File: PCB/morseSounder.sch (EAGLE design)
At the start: 77 parts, among them IC1 LM386M-1, IC5 LM321MF, J1 AVR_SPI_PRG_6PTH, J2 POWERPOLE_POWER25A_HORIZONTAL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, J3 POWER_JACKPTH, Q1 MMBT3904, Q2 MMBT3904, Q3 MMBT3904, Q4 2.5A/30V/105mΩ, Q5 MMBT3904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

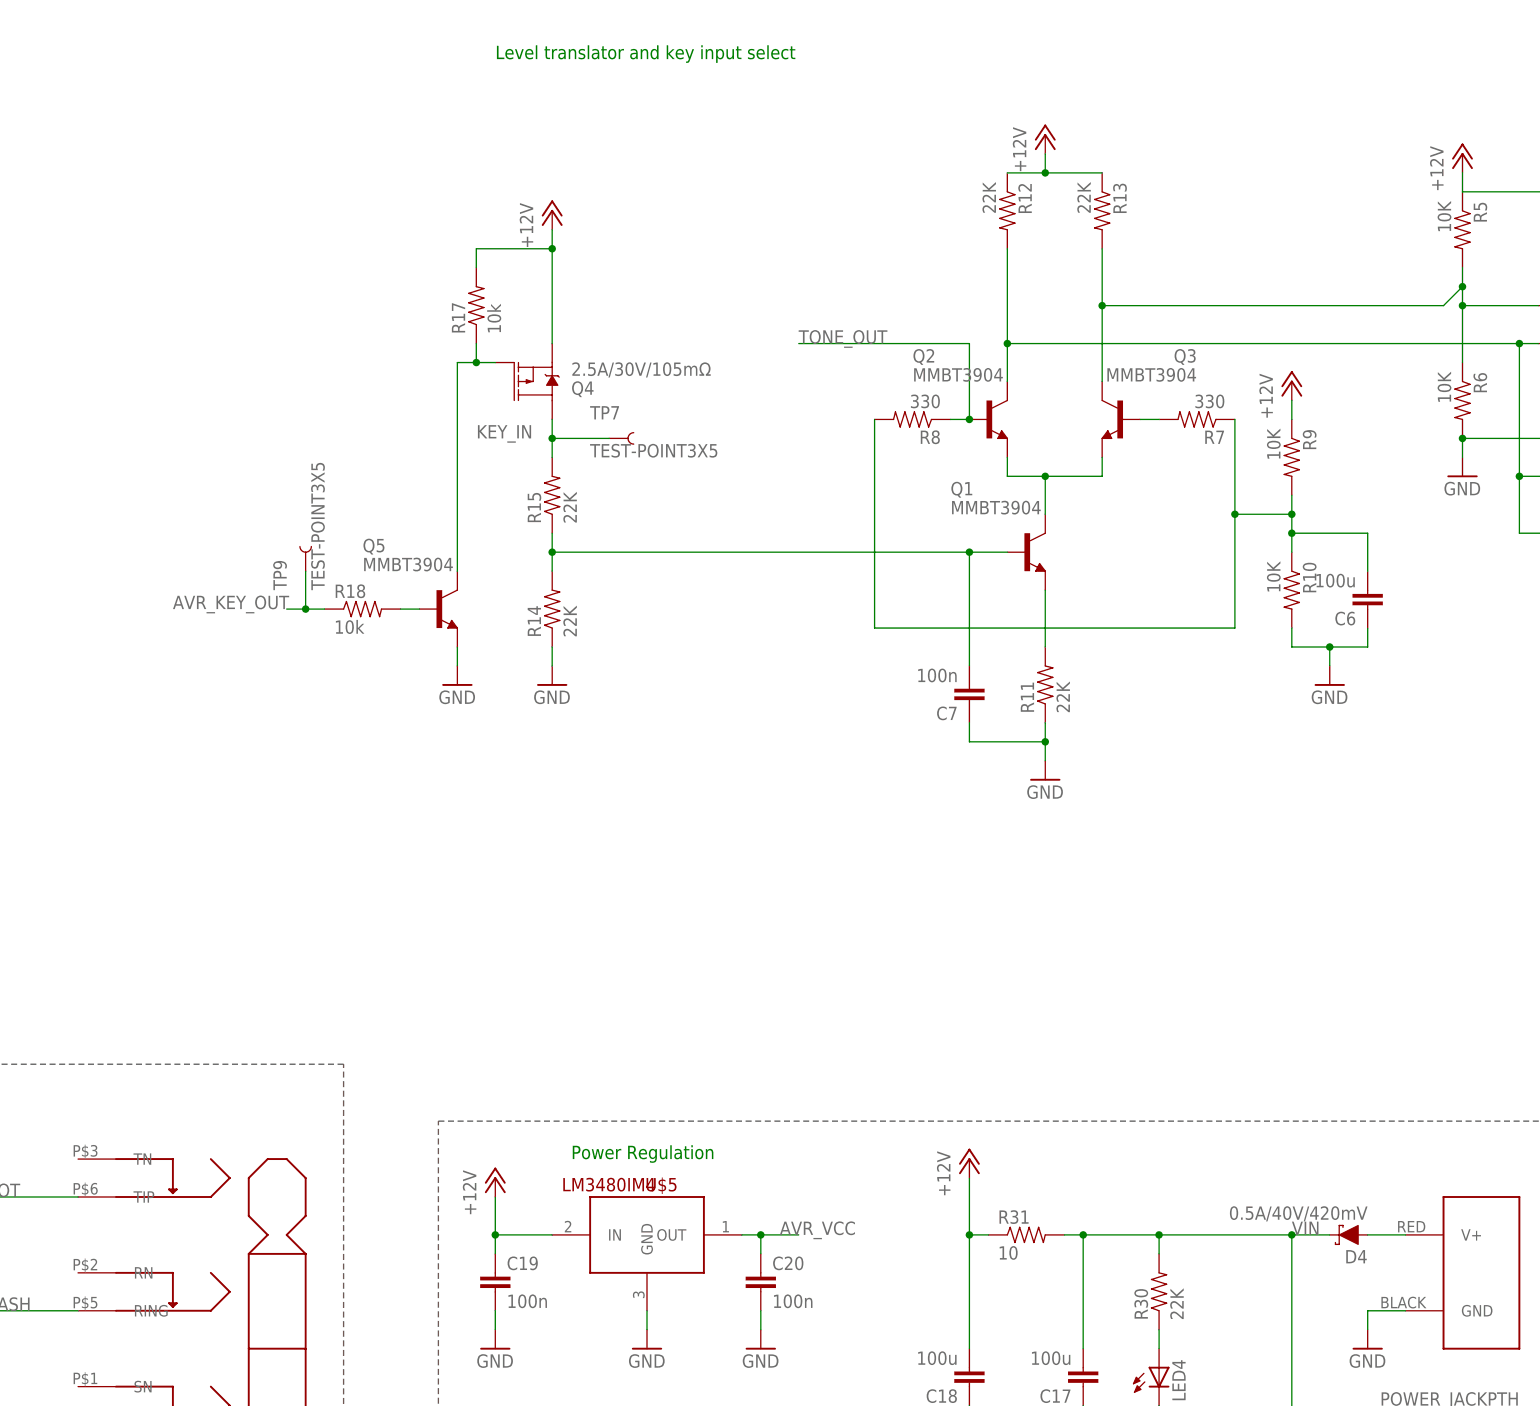
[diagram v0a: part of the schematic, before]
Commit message: * Oops! Power reverse protection diode should protect both power inputs!
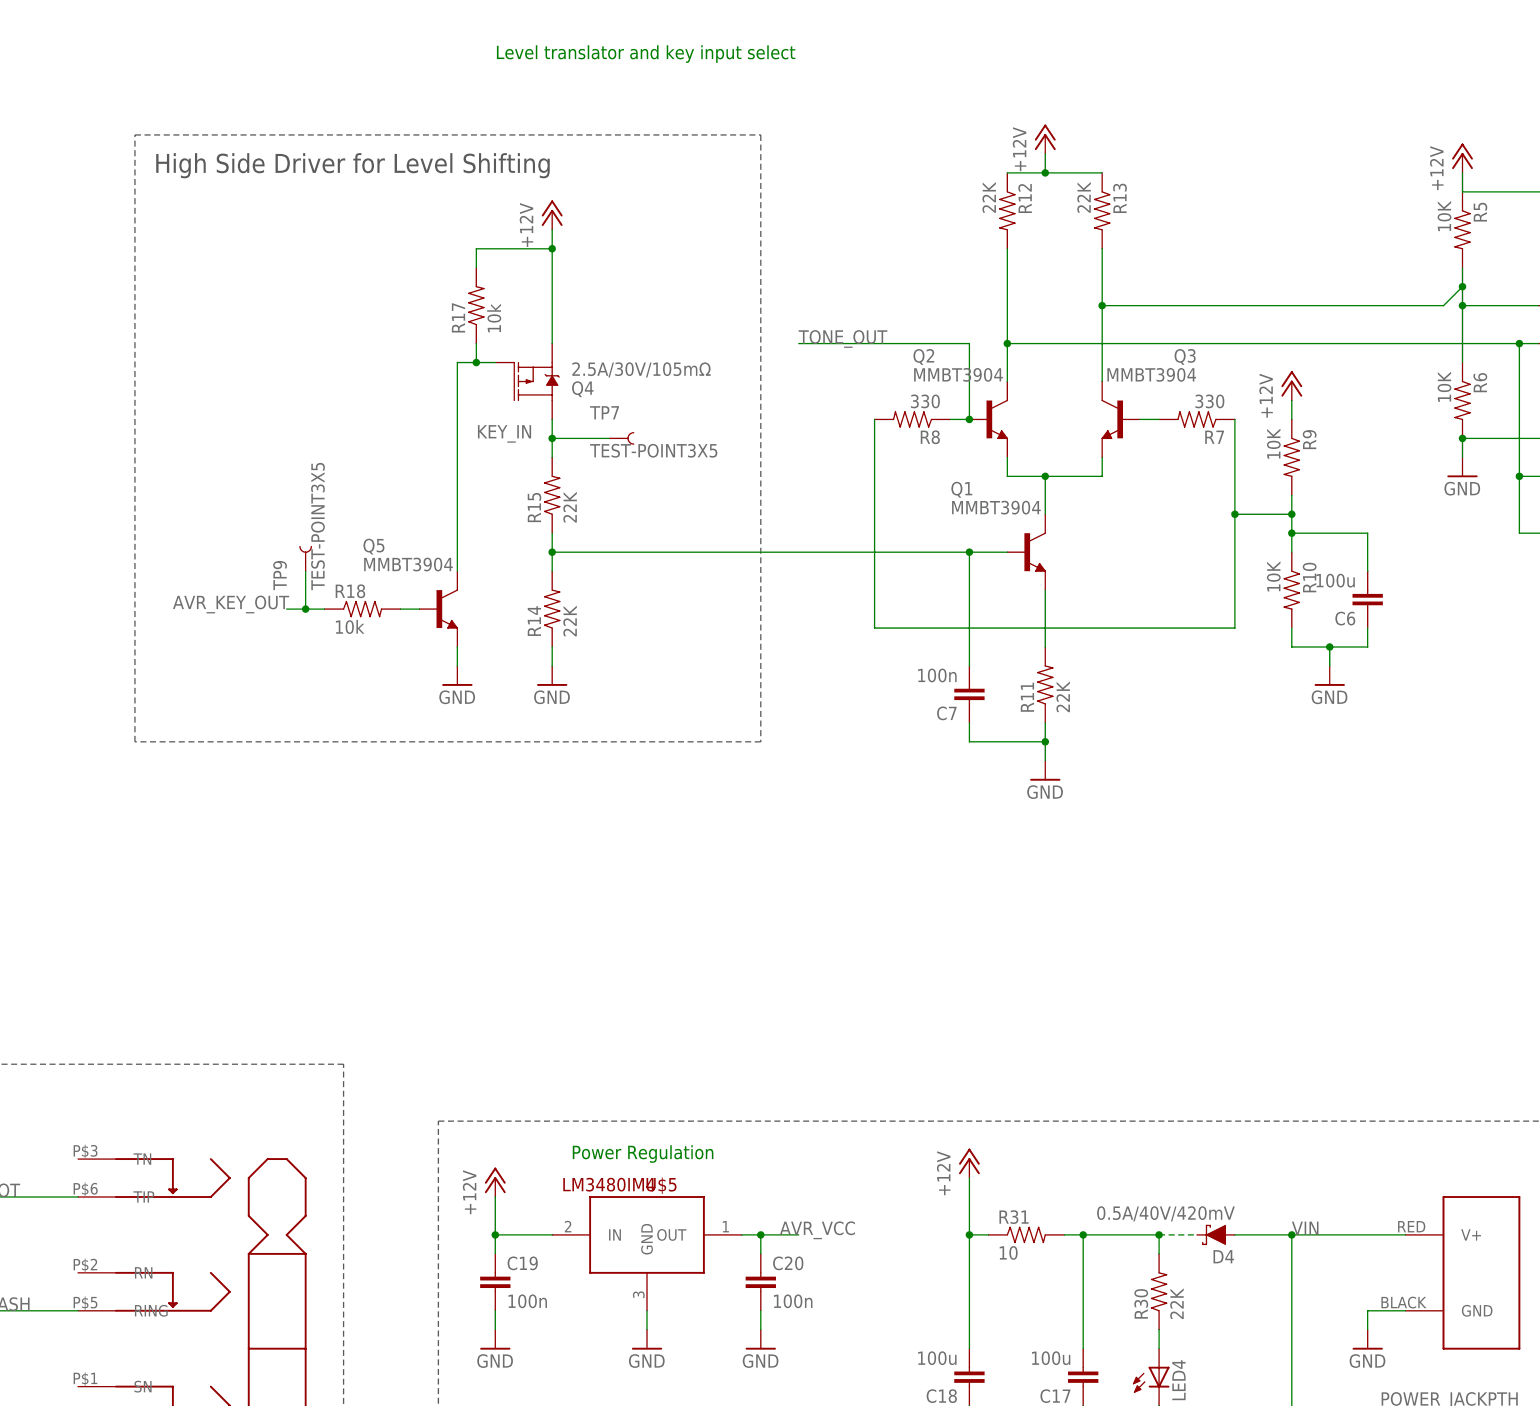
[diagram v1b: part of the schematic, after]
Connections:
- net N$4: now also C17.2, D4.C, R30.2, R31.2; no longer D4.A, J2.V+
- net VIN: now also D4.A, J2.V+; no longer C17.2, D4.C, R30.2, R31.2
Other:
- note added: "High Side Driver for Level Shifting"
- moved on the sheet: D4
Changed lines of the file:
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@@
 <wire x1="205.74" y1="-5.08" x2="119.38" y2="-5.08" width="0.1524" layer="97" style="longdash"/>
 <wire x1="119.38" y1="-5.08" x2="119.38" y2="-68.58" width="0.1524" layer="97" style="longdash"/>
+<wire x1="177.8" y1="119.38" x2="261.62" y2="119.38" width="0.1524" layer="97" style="longdash"/>
+<wire x1="261.62" y1="119.38" x2="261.62" y2="38.1" width="0.1524" layer="97" style="longdash"/>
+<wire x1="261.62" y1="38.1" x2="177.8" y2="38.1" width="0.1524" layer="97" style="longdash"/>
+<wire x1="177.8" y1="38.1" x2="177.8" y2="119.38" width="0.1524" layer="97" style="longdash"/>
+<text x="180.34" y="114.3" size="2.54" layer="97">High Side Driver for Level Shifting</text>
 </plain>
 <instances>
@@
 <instance part="D1" gate="G$1" x="139.7" y="-22.86" rot="R90"/>
 <instance part="D2" gate="G$1" x="127" y="-38.1" rot="R90"/>
-<instance part="D4" gate="G$1" x="340.36" y="-27.94" rot="R180"/>
+<instance part="D4" gate="G$1" x="322.58" y="-27.94" rot="R180"/>
 <instance part="GND10" gate="1" x="139.7" y="-53.34"/>
 <instance part="GND11" gate="1" x="127" y="-53.34"/>
@@
 <segment>
 <wire x1="332.74" y1="-53.34" x2="332.74" y2="-27.94" width="0.1524" layer="91"/>
-<wire x1="332.74" y1="-27.94" x2="314.96" y2="-27.94" width="0.1524" layer="91"/>
 <label x="332.74" y="-27.94" size="1.778" layer="95"/>
-<pinref part="R30" gate="G$1" pin="2"/>
-<wire x1="314.96" y1="-30.48" x2="314.96" y2="-27.94" width="0.1524" layer="91"/>
-<pinref part="R31" gate="G$1" pin="2"/>
-<wire x1="314.96" y1="-27.94" x2="304.8" y2="-27.94" width="0.1524" layer="91"/>
-<junction x="314.96" y="-27.94"/>
-<pinref part="C17" gate="G$1" pin="2"/>
-<wire x1="304.8" y1="-43.18" x2="304.8" y2="-27.94" width="0.1524" layer="91"/>
-<wire x1="304.8" y1="-27.94" x2="302.26" y2="-27.94" width="0.1524" layer="91"/>
-<junction x="304.8" y="-27.94"/>
 <pinref part="J3" gate="G$1" pin="PWR"/>
 <wire x1="350.52" y1="-53.34" x2="332.74" y2="-53.34" width="0.1524" layer="91"/>
-<pinref part="D4" gate="G$1" pin="C"/>
-<wire x1="337.82" y1="-27.94" x2="332.74" y2="-27.94" width="0.1524" layer="91"/>
+<pinref part="D4" gate="G$1" pin="A"/>
+<wire x1="325.12" y1="-27.94" x2="332.74" y2="-27.94" width="0.1524" layer="91"/>
+<pinref part="J2" gate="G$1" pin="V+"/>
+<wire x1="347.98" y1="-27.94" x2="332.74" y2="-27.94" width="0.1524" layer="91"/>
 <junction x="332.74" y="-27.94"/>
 </segment>
@@
 </segment>
 </net>
-<net name="N$4" class="0">
-<segment>
-<pinref part="D4" gate="G$1" pin="A"/>
-<pinref part="J2" gate="G$1" pin="V+"/>
-<wire x1="342.9" y1="-27.94" x2="347.98" y2="-27.94" width="0.1524" layer="91"/>
-</segment>
-</net>
 <net name="N$17" class="0">
 <segment>
@@
 </segment>
 </net>
+<net name="N$4" class="0">
+<segment>
+<pinref part="R31" gate="G$1" pin="2"/>
+<pinref part="R30" gate="G$1" pin="2"/>
+<wire x1="314.96" y1="-30.48" x2="314.96" y2="-27.94" width="0.1524" layer="91"/>
+<wire x1="314.96" y1="-27.94" x2="304.8" y2="-27.94" width="0.1524" layer="91"/>
+<wire x1="304.8" y1="-27.94" x2="302.26" y2="-27.94" width="0.1524" layer="91"/>
+<junction x="304.8" y="-27.94"/>
+<pinref part="C17" gate="G$1" pin="2"/>
+<wire x1="304.8" y1="-43.18" x2="304.8" y2="-27.94" width="0.1524" layer="91"/>
+<pinref part="D4" gate="G$1" pin="C"/>
+<wire x1="314.96" y1="-27.94" x2="320.04" y2="-27.94" width="0.1524" layer="91" style="longdash"/>
+<junction x="314.96" y="-27.94"/>
+</segment>
+</net>

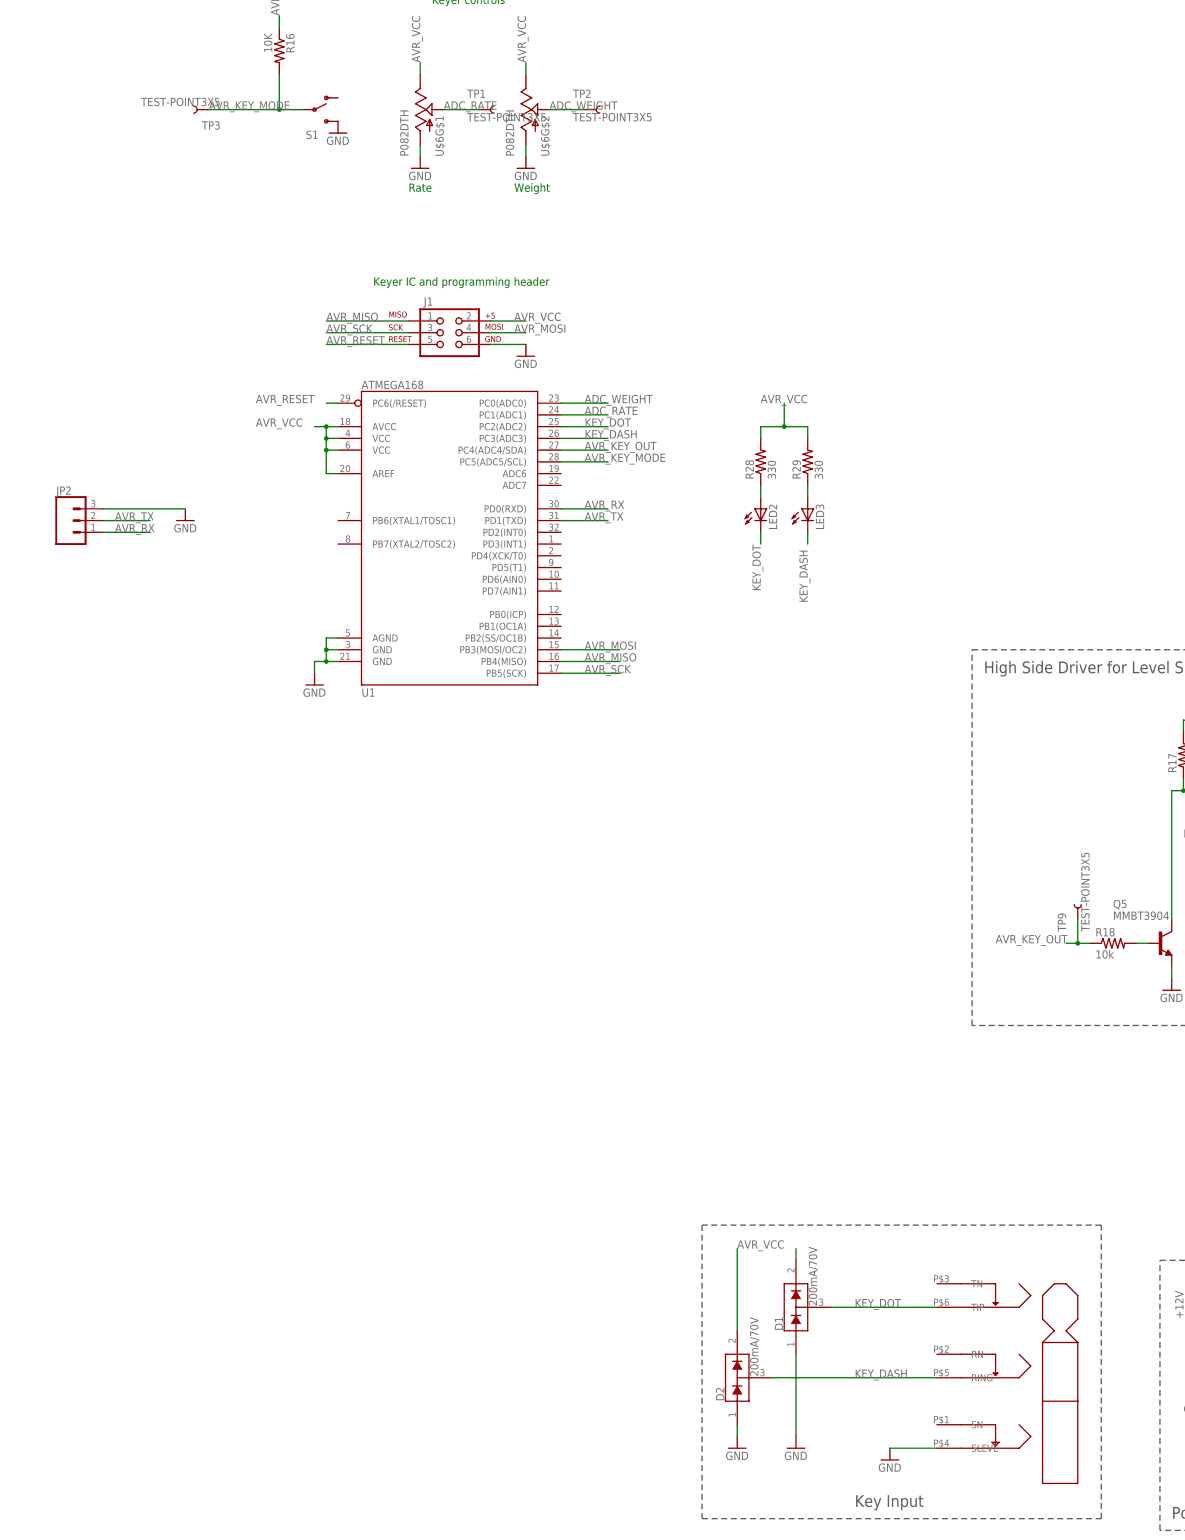
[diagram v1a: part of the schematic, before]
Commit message: Routed rest of PCB
Altered pin placement on AVR
Added additional protection to key input
Separated LEDS from key input
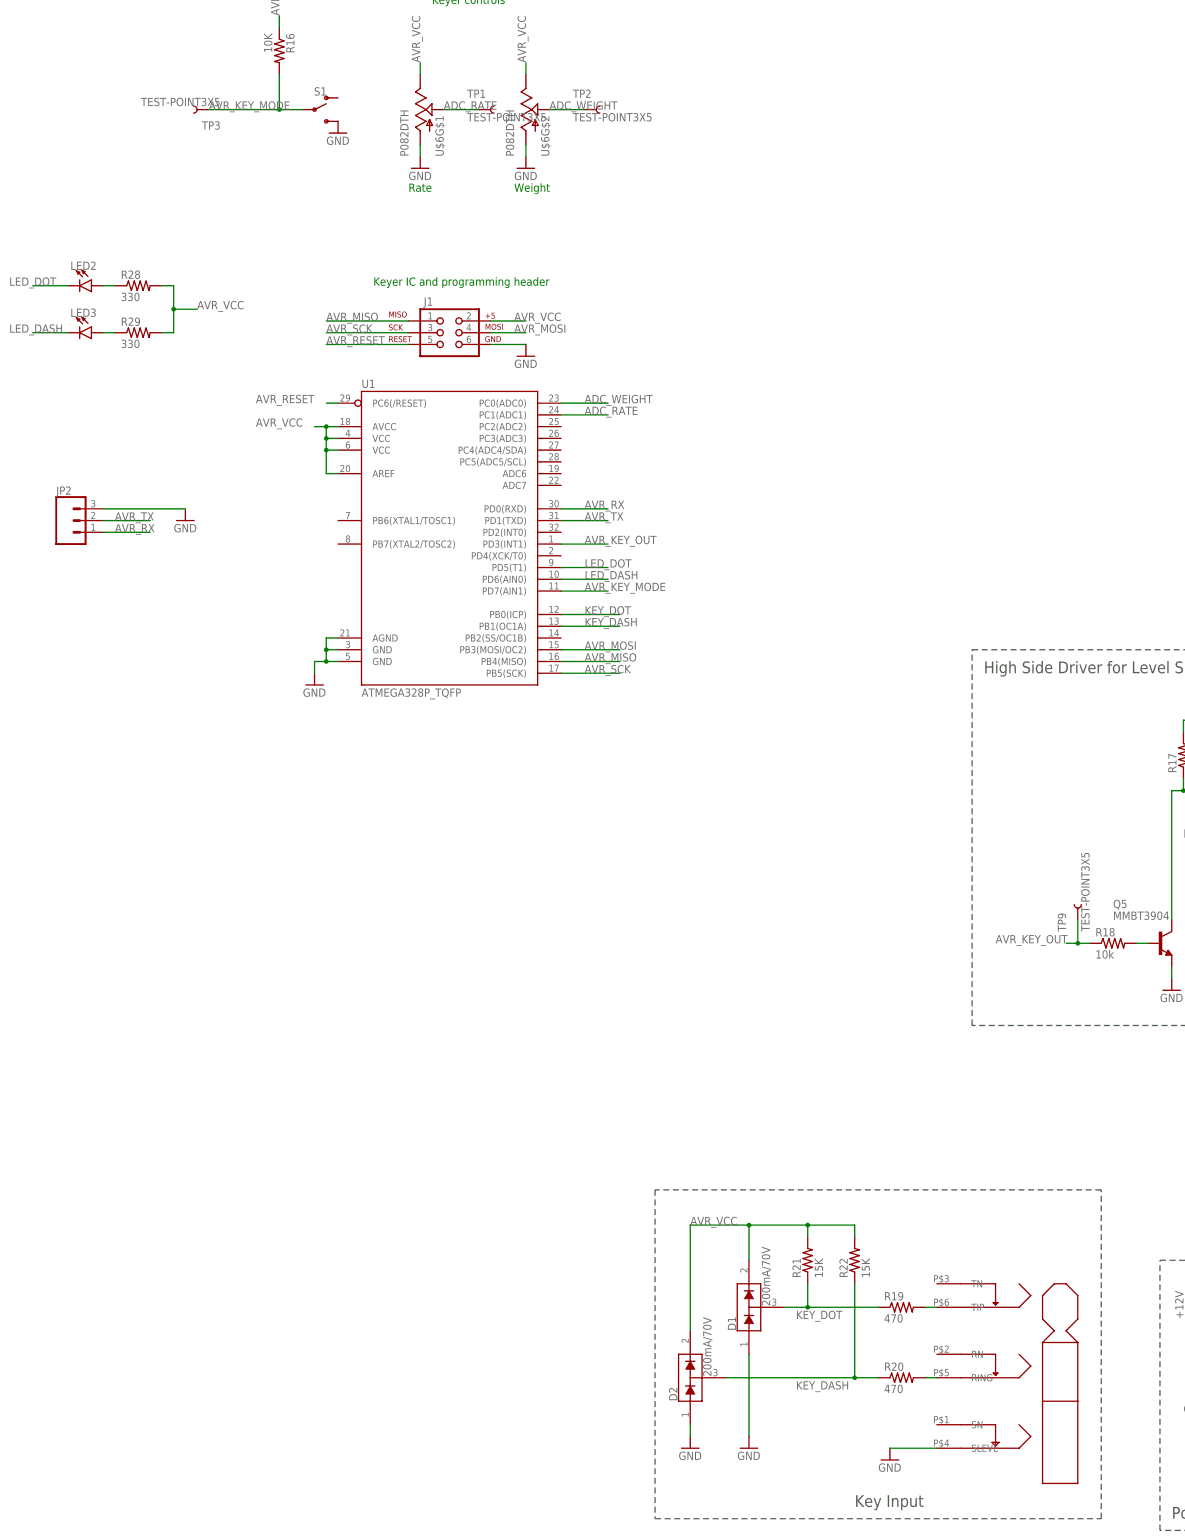
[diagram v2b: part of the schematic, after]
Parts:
- added R19, R20: 470, SparkFun:RESISTOR0805-RES
- added R21, R22: 15K, SparkFun:RESISTOR0805-RES
- LED2, LED3: device SparkFun:LED-3MM-NO_SILK -> SparkFun-LED:LED-RED1206
- S1: device SparkFun:SWITCH-SPSTSMD2 -> morseSounder:SWITCH-SPDTTE-1825232-1
- U1: value ATMEGA168 -> ATMEGA328P_TQFP; device SparkFun:ATMEGA168 -> SparkFun-IC-Microcontroller:ATMEGA328P_TQFP
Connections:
- new net LED_DASH: LED3.C, U1.PD6(AIN0)
- new net LED_DOT: LED2.C, U1.PD5(T1)
- new net N$10: R20.2, U$1.RING
- new net N$18: R19.2, U$1.TIP
- net AVR_KEY_MODE: now also U1.PD7(AIN1); no longer U1.PC5(ADC5/SCL)
- net AVR_KEY_OUT: now also U1.PD3(INT1); no longer U1.PC4(ADC4/SDA)
- net AVR_VCC: now also R21.2, R22.2, U1.VCC@4, U1.VCC@6; no longer U1.VCC@1, U1.VCC@2
- net GND: now also U1.GND@3, U1.GND@5; no longer U1.GND@1, U1.GND@2
- net KEY_DASH: now also R20.1, R22.1, U1.PB1(OC1A); no longer LED3.C, U$1.RING, U1.PC3(ADC3)
- net KEY_DOT: now also R19.1, R21.1, U1.PB0(ICP); no longer LED2.C, U$1.TIP, U1.PC2(ADC2)
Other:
- moved on the sheet: D1, D2, R28, R29
